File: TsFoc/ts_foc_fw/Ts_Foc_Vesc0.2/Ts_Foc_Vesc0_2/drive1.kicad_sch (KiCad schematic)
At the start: 31 parts, among them Q2 RU3089M-C, Q3 RU3089M-C, Q4 RU3089M-C, Q5 RU3089M-C, Q6 RU3089M-C, Q7 RU3089M-C, U4 EG2133, U5 INA240A2PWR, U6 INA240A2PWR

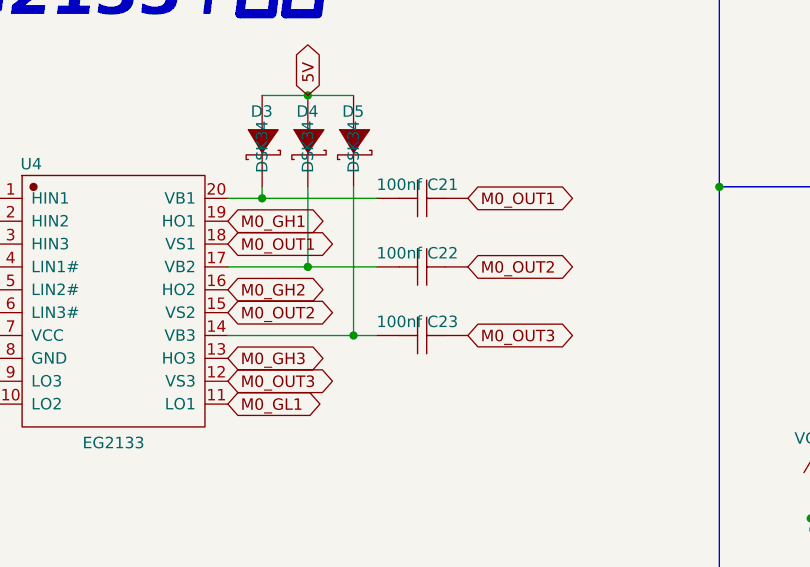
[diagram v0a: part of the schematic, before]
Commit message: 1. can通信测试通过 2. as5600通信测试通过 3. PCB板桥驱动电路有标签错误，导致有四个引脚未能链接 4.
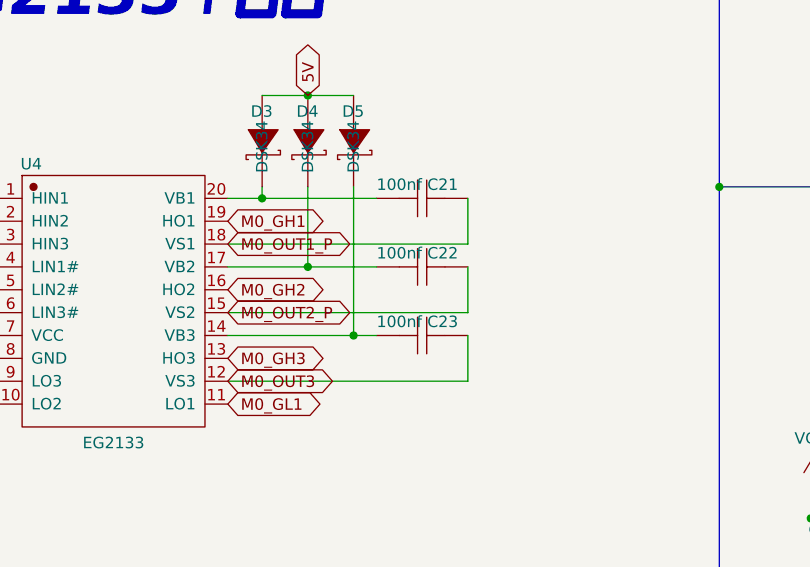
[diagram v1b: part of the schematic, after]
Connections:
- net M0_OUT1 is gone; now on net M0_OUT1_P: C21.1, U4.18 (VS1)
- net M0_OUT2 is gone; now on net M0_OUT2_P: C22.1, U4.15 (VS2)
